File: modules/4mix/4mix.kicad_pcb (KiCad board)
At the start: 2 copper layers, 91.4 x 68.6 mm, 104 parts, among them U1 MCP6002-xSN, U2 MCP6002-xSN, U3 MCP6002-xSN, U4 MCP6002-xSN, U5 MCP6002-xSN, U6 MCP6002-xSN, U7 MCP6002-xSN, U8 MCP6002-xSN

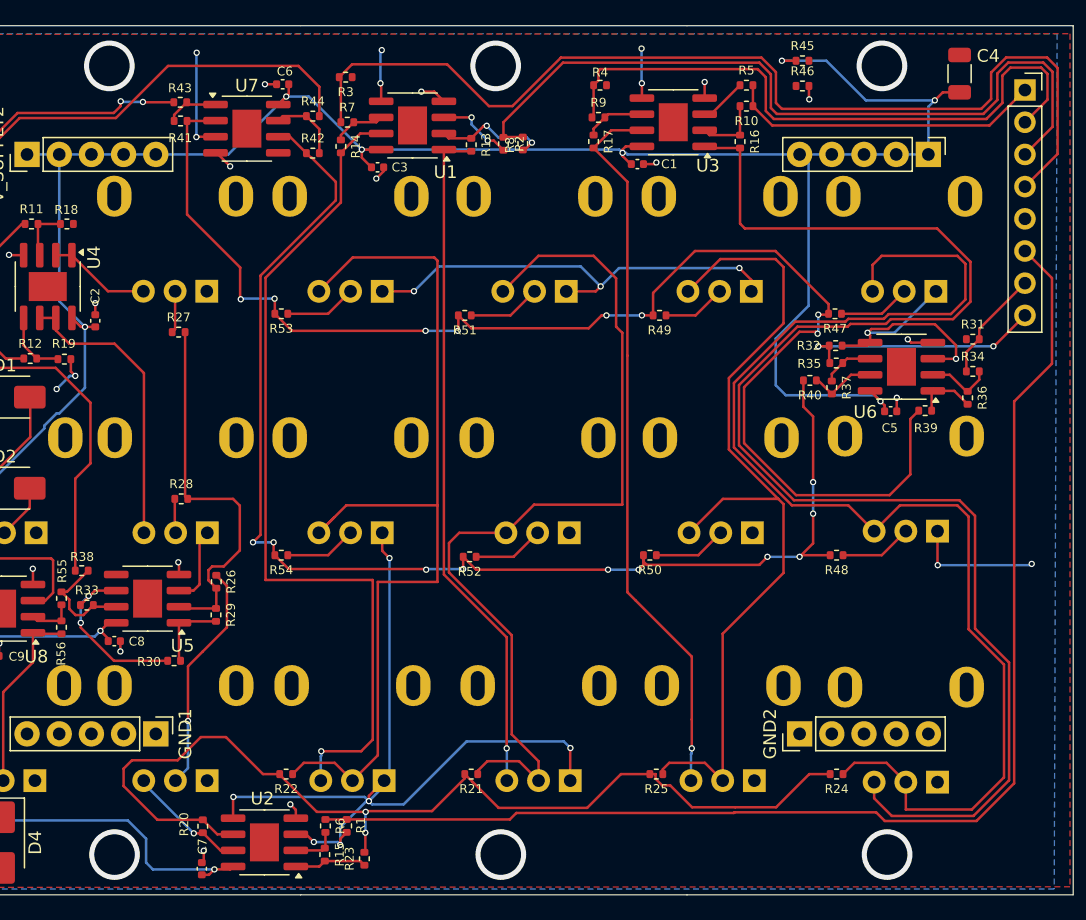
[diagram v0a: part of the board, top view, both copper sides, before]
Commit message: 4mix: Fix leaky ch1 sendA routing Also change the mounting hole positions to match mirroring
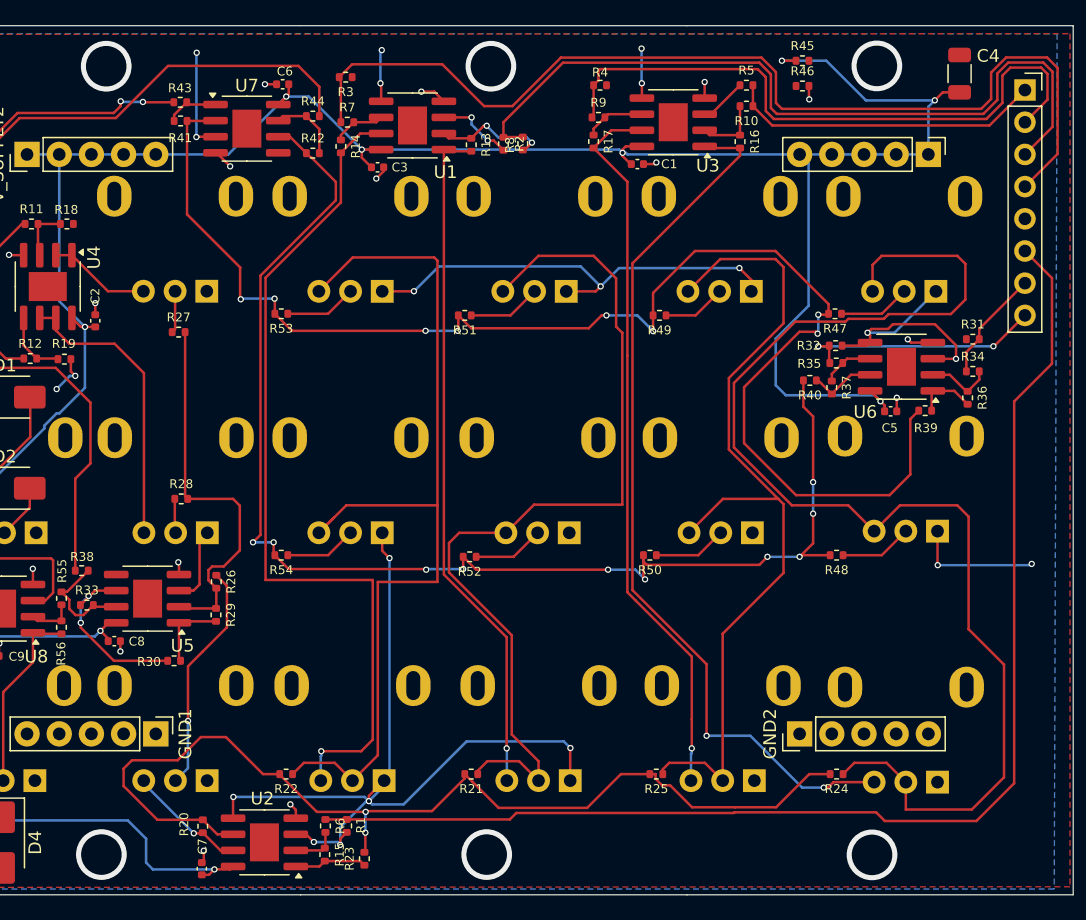
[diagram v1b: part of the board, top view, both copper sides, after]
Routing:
- net Net-(R16-Pad2): track 113.7 -> 70.3 mm, vias 0 -> 2
- net SEND_A_MIX: track 109.2 -> 110.9 mm
- net SEND_B_MIX: track 102.1 -> 103.6 mm
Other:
- board text added: "4MIX 0.3.0"
- board text removed: "4MIX 0.2.0"

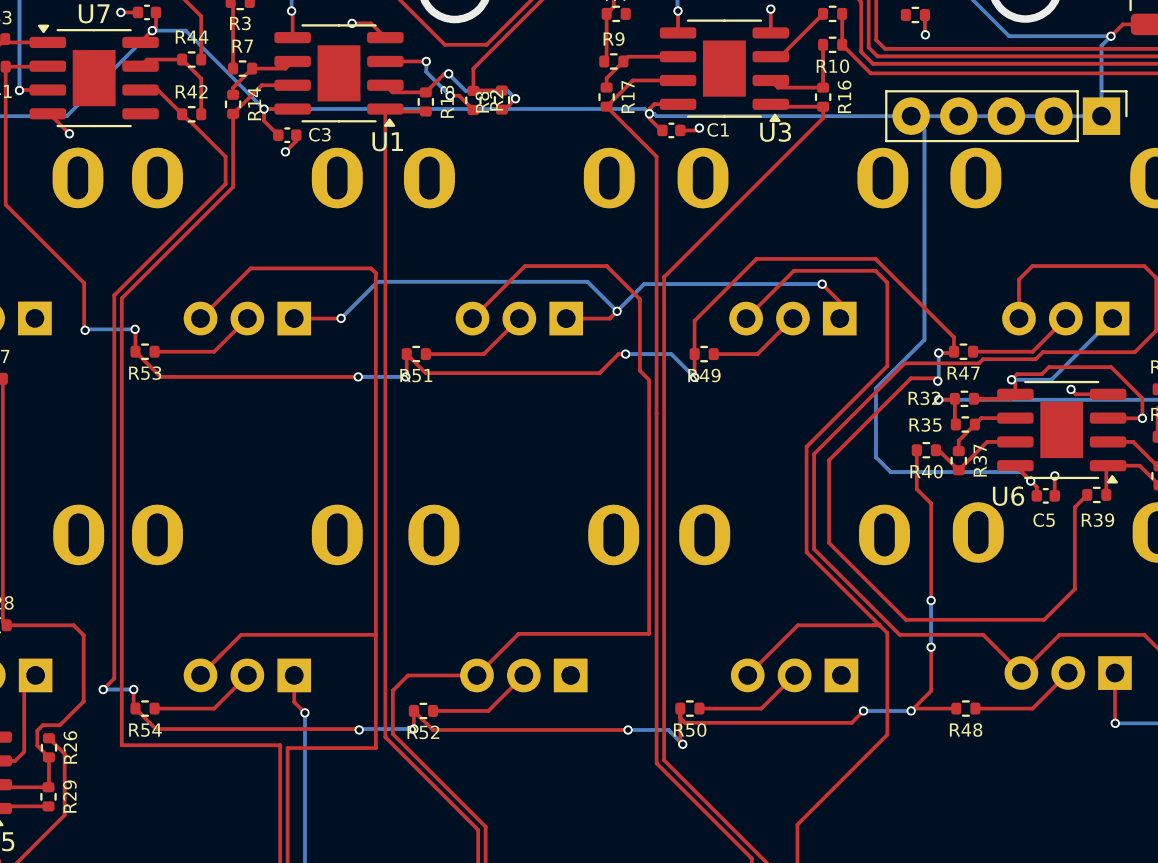
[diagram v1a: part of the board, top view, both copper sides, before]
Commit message: 4mix: Fixing ch4 send-b leakage.
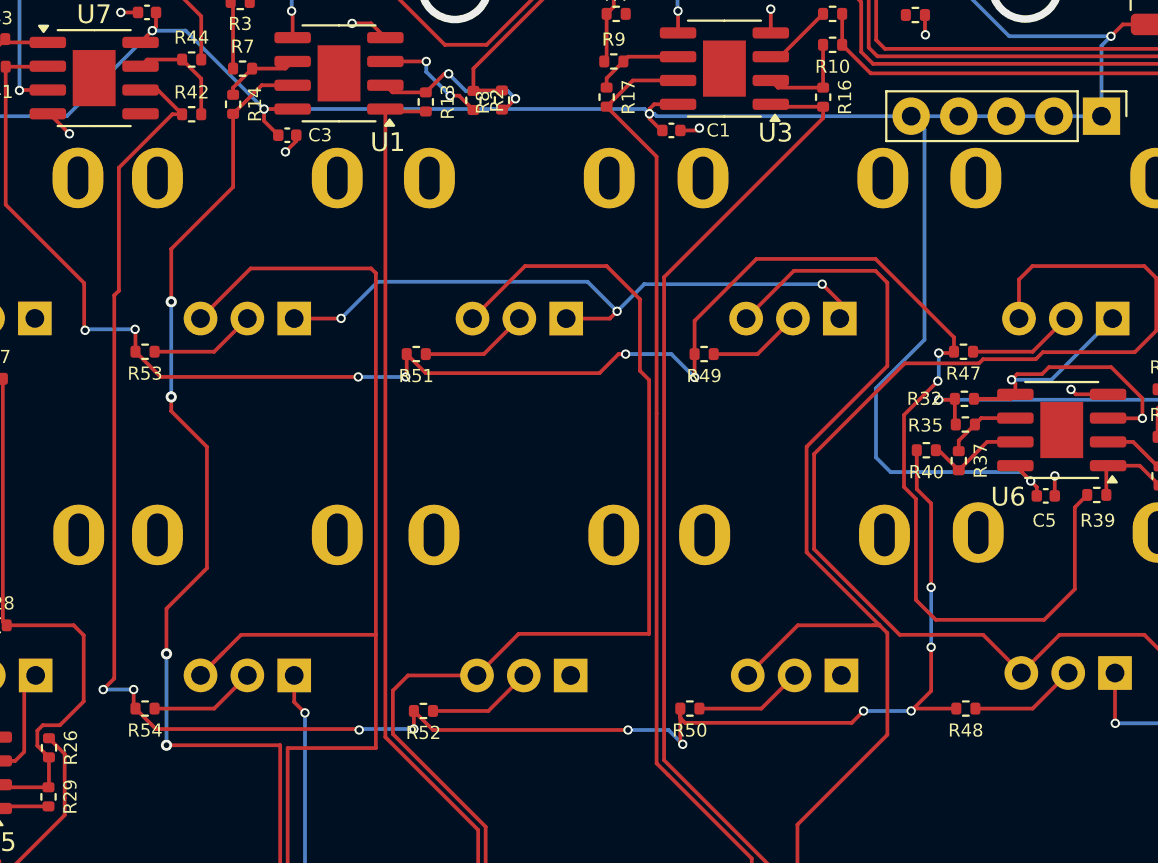
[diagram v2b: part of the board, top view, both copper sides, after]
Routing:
- net SEND_A_MIX: track 110.9 -> 105.6 mm
- net Net-(R14-Pad2): track 67.8 -> 66.0 mm, vias 1 -> 5
- net SEND_B_MIX: track 103.6 -> 101.9 mm
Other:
- board text added: "4MIX 0.4.0"
- board text removed: "4MIX 0.3.0"
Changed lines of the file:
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@@
 		)
 	)
-	(gr_text "4MIX\n0.3.0"
+	(gr_text "4MIX\n0.4.0"
 		(at 48.387 107.95 0)
 		(layer "B.SilkS")
@@
 	)
 	(segment
-		(start 116.561772 77.686)
-		(end 123.9392 77.686)
-		(width 0.2)
-		(layer "F.Cu")
-		(net 37)
-	)
-	(segment
-		(start 112.4584 69.165372)
-		(end 112.4584 73.582628)
-		(width 0.2)
-		(layer "F.Cu")
-		(net 37)
-	)
-	(segment
 		(start 108.585 58.42)
 		(end 105.279 61.726)
@@
 	)
 	(segment
+		(start 117.094 71.228486)
+		(end 117.094 76.622218)
+		(width 0.2)
+		(layer "F.Cu")
+		(net 37)
+	)
+	(segment
 		(start 76.7802 64.7192)
 		(end 75.434 63.373)
@@
 	)
 	(segment
-		(start 125.5772 76.048)
-		(end 125.5772 71.6792)
-		(width 0.2)
-		(layer "F.Cu")
-		(net 37)
-	)
-	(segment
 		(start 68.5058 48.1584)
 		(end 68.5058 55.5264)
@@
 	)
 	(segment
-		(start 116.830772 64.793)
-		(end 112.4584 69.165372)
+		(start 116.459 66.7464)
+		(end 116.459 70.593486)
 		(width 0.2)
 		(layer "F.Cu")
@@
 	)
 	(segment
+		(start 116.459 70.593486)
+		(end 117.094 71.228486)
+		(width 0.2)
+		(layer "F.Cu")
+		(net 37)
+	)
+	(segment
 		(start 114.935 58.42)
 		(end 108.585 58.42)
@@
 	)
 	(segment
+		(start 117.094 76.622218)
+		(end 118.157782 77.686)
+		(width 0.2)
+		(layer "F.Cu")
+		(net 37)
+	)
+	(segment
+		(start 118.157782 77.686)
+		(end 123.9392 77.686)
+		(width 0.2)
+		(layer "F.Cu")
+		(net 37)
+	)
+	(segment
 		(start 119.124 62.609)
 		(end 114.935 58.42)
@@
 	)
 	(segment
-		(start 112.4584 73.582628)
-		(end 116.561772 77.686)
-		(width 0.2)
-		(layer "F.Cu")
-		(net 37)
-	)
-	(segment
 		(start 75.434 62.2006)
 		(end 75.434 63.373)
@@
 	)
 	(segment
-		(start 119.054 63.443)
-		(end 119.124 63.373)
+		(start 118.2624 64.943)
+		(end 116.459 66.7464)
 		(width 0.2)
 		(layer "F.Cu")
@@
 	)
 	(segment
-		(start 123.9392 77.686)
-		(end 125.5772 76.048)
+		(start 119.054 63.443)
+		(end 119.124 63.373)
 		(width 0.2)
 		(layer "F.Cu")
@@
 	)
 	(segment
-		(start 118.2624 64.943)
-		(end 118.1124 64.793)
+		(start 125.5772 76.048)
+		(end 125.5772 71.6792)
 		(width 0.2)
 		(layer "F.Cu")
@@
 	)
 	(segment
-		(start 125.5772 71.6792)
-		(end 126.238 71.0184)
+		(start 123.9392 77.686)
+		(end 125.5772 76.048)
 		(width 0.2)
 		(layer "F.Cu")
@@
 	)
 	(segment
-		(start 101.6 63.5)
-		(end 101.219 63.5)
+		(start 125.5772 71.6792)
+		(end 126.238 71.0184)
 		(width 0.2)
 		(layer "F.Cu")
@@
 	)
 	(segment
-		(start 118.1124 64.793)
-		(end 116.830772 64.793)
+		(start 101.6 63.5)
+		(end 101.219 63.5)
 		(width 0.2)
 		(layer "F.Cu")
@@
 	)
 	(segment
+		(start 104.775 83.185)
+		(end 104.517 82.927)
+		(width 0.2)
+		(layer "F.Cu")
+		(net 41)
+	)
+	(segment
 		(start 117.9068 71.4756)
-		(end 117.9068 76.6572)
+		(end 117.1408 70.7096)
 		(width 0.2)
 		(layer "F.Cu")
@@
 	)
 	(segment
-		(start 104.775 83.185)
-		(end 104.517 82.927)
+		(start 74.3014 60.362514)
+		(end 74.549 60.114914)
 		(width 0.2)
 		(layer "F.Cu")
@@
 	)
 	(segment
-		(start 117.1408 68.6308)
-		(end 117.1408 70.7096)
+		(start 117.1408 70.7096)
+		(end 117.1408 68.6308)
 		(width 0.2)
 		(layer "F.Cu")
@@
 	)
 	(segment
+		(start 73.7108 81.407)
+		(end 74.3014 80.8164)
+		(width 0.2)
+		(layer "F.Cu")
+		(net 41)
+	)
+	(segment
 		(start 76.5262 83.5152)
 		(end 75.434 82.423)
@@
 	)
 	(segment
-		(start 80.245 54.418914)
-		(end 80.245 52.9654)
-		(width 0.2)
-		(layer "F.Cu")
-		(net 41)
-	)
-	(segment
-		(start 74.3014 60.362514)
-		(end 80.245 54.418914)
+		(start 74.549 60.114914)
+		(end 74.549 53.552405)
 		(width 0.2)
 		(layer "F.Cu")
@@
 	)
 	(segment
-		(start 104.517 84.197)
-		(end 104.517 82.423)
+		(start 74.549 53.552405)
+		(end 77.403005 50.6984)
 		(width 0.2)
 		(layer "F.Cu")
@@
 	)
 	(segment
-		(start 73.7108 81.407)
-		(end 74.3014 80.8164)
+		(start 117.9068 75.946)
+		(end 117.9068 71.4756)
 		(width 0.2)
 		(layer "F.Cu")
@@
 	)
 	(segment
-		(start 117.9068 79.1464)
-		(end 117.9068 81.4832)
+		(start 104.517 84.197)
+		(end 104.517 82.423)
 		(width 0.2)
 		(layer "F.Cu")
@@
 	)
 	(segment
-		(start 117.1408 70.7096)
-		(end 117.9068 71.4756)
+		(start 117.9068 79.1464)
+		(end 117.9068 81.4832)
 		(width 0.2)
 		(layer "F.Cu")
@@
 	)
 	(segment
-		(start 78.267 51.0422)
-		(end 77.9232 50.6984)
+		(start 74.3014 80.8164)
+		(end 74.3014 60.362514)
 		(width 0.2)
 		(layer "F.Cu")
@@
 	)
 	(segment
-		(start 80.245 52.9654)
-		(end 78.3218 51.0422)
+		(start 76.6278 49.403)
+		(end 75.7032 49.403)
 		(width 0.2)
 		(layer "F.Cu")
@@
 	)
 	(segment
-		(start 76.6278 49.403)
-		(end 75.7032 49.403)
+		(start 77.403005 50.6984)
+		(end 77.9232 50.6984)
 		(width 0.2)
 		(layer "F.Cu")
@@
 	)
 	(segment
-		(start 78.3218 51.0422)
-		(end 78.267 51.0422)
-		(width 0.2)
-		(layer "F.Cu")
-		(net 41)
-	)
-	(segment
 		(start 116.967 82.423)
 		(end 116.84 82.55)
@@
 	)
 	(segment
-		(start 74.3014 80.8164)
-		(end 74.3014 60.362514)
-		(width 0.2)
-		(layer "F.Cu")
-		(net 41)
-	)
-	(segment
 		(start 114.3 82.55)
 		(end 113.665 83.185)
@@
 	)
 	(via
-		(at 117.9068 76.6572)
+		(at 117.9068 75.946)
 		(size 0.5)
 		(drill 0.3)
@@
 	)
 	(segment
-		(start 73.7108 81.407)
-		(end 75.3364 81.407)
+		(start 117.9068 75.946)
+		(end 117.9068 79.1464)
 		(width 0.2)
 		(layer "B.Cu")
@@
 	)
 	(segment
-		(start 116.84 82.55)
-		(end 114.3 82.55)
+		(start 73.7108 81.407)
+		(end 75.3364 81.407)
 		(width 0.2)
 		(layer "B.Cu")
@@
 	)
 	(segment
-		(start 117.9068 76.6572)
-		(end 117.9068 79.1464)
+		(start 116.84 82.55)
+		(end 114.3 82.55)
 		(width 0.2)
 		(layer "B.Cu")
@@
 	)
 	(segment
+		(start 79.248 68.453)
+		(end 79.248 74.93)
+		(width 0.2)
+		(layer "F.Cu")
+		(net 45)
+	)
+	(segment
+		(start 77.343 57.8866)
+		(end 77.343 60.706)
+		(width 0.2)
+		(layer "F.Cu")
+		(net 45)
+	)
+	(segment
+		(start 77.089 77.089)
+		(end 77.089 79.502)
+		(width 0.2)
+		(layer "F.Cu")
+		(net 45)
+	)
+	(segment
 		(start 80.645 50.677)
 		(end 82.173 49.149)
@@
 	)
 	(segment
-		(start 74.7014 84.3788)
-		(end 83.157 84.3788)
+		(start 80.645 54.5846)
+		(end 77.343 57.8866)
+		(width 0.2)
+		(layer "F.Cu")
+		(net 45)
+	)
+	(segment
+		(start 77.343 66.548)
+		(end 79.248 68.453)
+		(width 0.2)
+		(layer "F.Cu")
+		(net 45)
+	)
+	(segment
+		(start 79.121 75.057)
+		(end 77.089 77.089)
 		(width 0.2)
 		(layer "F.Cu")
@@
 	)
 	(segment
-		(start 80.645 54.5846)
-		(end 74.7014 60.5282)
+		(start 79.248 74.93)
+		(end 79.121 75.057)
 		(width 0.2)
 		(layer "F.Cu")
@@
 	)
 	(segment
-		(start 74.7014 60.5282)
-		(end 74.7014 84.3788)
+		(start 77.089 84.3788)
+		(end 83.157 84.3788)
+		(width 0.2)
+		(layer "F.Cu")
+		(net 45)
+	)
+	(segment
+		(start 77.343 65.786)
+		(end 77.343 66.548)
 		(width 0.2)
 		(layer "F.Cu")
@@
 	)
 	(via
+		(at 77.089 84.3788)
+		(size 0.6)
+		(drill 0.3)
+		(layers "F.Cu" "B.Cu")
+		(net 45)
+	)
+	(via
 		(at 79.0956 97.8916)
 		(size 0.5)
@@
 		(net 45)
 	)
+	(via
+		(at 77.089 79.502)
+		(size 0.6)
+		(drill 0.3)
+		(layers "F.Cu" "B.Cu")
+		(net 45)
+	)
+	(via
+		(at 77.343 65.786)
+		(size 0.6)
+		(drill 0.3)
+		(layers "F.Cu" "B.Cu")
+		(net 45)
+	)
+	(via
+		(at 77.343 60.706)
+		(size 0.6)
+		(drill 0.3)
+		(layers "F.Cu" "B.Cu")
+		(net 45)
+	)
+	(segment
+		(start 77.343 60.706)
+		(end 77.343 65.786)
+		(width 0.2)
+		(layer "B.Cu")
+		(net 45)
+	)
+	(segment
+		(start 77.089 79.502)
+		(end 77.089 84.3788)
+		(width 0.2)
+		(layer "B.Cu")
+		(net 45)
+	)

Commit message: Finished the new schematic for 4mix
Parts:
- removed C1, C2, C3, C5, C6, C7, C8, C9: 0.1uf, Capacitor_SMD:C_0402_1005Metric
- removed C4: 100uf, Capacitor_SMD:C_1206_3216Metric
- removed D1, D2, D3: SS14, Diode_SMD:D_SMA
- removed D4: SS210, Diode_SMD:D_SMA
- removed R1, R18, R19, R2, R3, R31, R32, R39, R4, R40, R41, R42, R47, R48, R49, R5, R50, R51, R52, R53, R54: 1M, Resistor_SMD:R_0402_1005Metric
- removed R10, R11, R12, R13, R14, R15, R16, R17, R30, R33, R34, R35, R36, R37, R55, R56, R6, R7, R8, R9: 100k, Resistor_SMD:R_0402_1005Metric
- removed R20, R21, R22, R23, R24, R25, R26, R27, R28, R29: 200k, Resistor_SMD:R_0402_1005Metric
- removed R38, R43, R44, R45, R46, R57, R59, R60: 1k, Resistor_SMD:R_0402_1005Metric
- removed R58: 51k, Resistor_SMD:R_0402_1005Metric
- removed RV1, RV16, RV2, RV3, RV4, RV5, RV6, RV7: 50k, BreadModular_Pots:Potentiometer_RV09
- removed RV10, RV11, RV12, RV13, RV14, RV15, RV17, RV8, RV9: 500k, BreadModular_Pots:Potentiometer_RV09
- removed U1, U2, U3, U4, U5, U6, U7, U8: MCP6002-xSN, Package_SO:SOIC-8-1EP_3.9x4.9mm_P1.27mm_EP2.29x3mm
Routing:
- net V_SUPPLY: track 240.0 -> 0.00 mm, vias 10 -> 0
- net V_MID: track 180.1 -> 0.00 mm, vias 24 -> 1
- net SEND_A_MIX: track 105.6 -> 0.00 mm, vias 8 -> 0
- net SEND_B_MIX: track 101.9 -> 0.00 mm, vias 10 -> 0
- net IN_MIXOUT: track 100.2 -> 0.00 mm
- net /SENDS/INPUT: track 100.1 -> 0.00 mm
- net IN_4: track 80.4 -> 0.00 mm
- net MAIN_MIX: track 80.1 -> 0.00 mm, vias 2 -> 0
- net /SENDS3/INPUT: track 74.8 -> 0.00 mm
- net /SENDS2/INPUT: track 71.5 -> 0.00 mm
- net Net-(R16-Pad2): track 70.3 -> 0.00 mm, vias 2 -> 0
- net /SENDS1/INPUT: track 69.3 -> 0.00 mm
- net Net-(R14-Pad2): track 66.0 -> 0.00 mm, vias 5 -> 0
- net IN_3: track 61.9 -> 0.00 mm
- net Net-(R17-Pad2): track 57.5 -> 0.00 mm, vias 1 -> 0
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- removed copper zone on B.Cu, net GND
- removed copper zone on F.Cu, net V_MID
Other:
- board text removed: "CH-1"
- board text removed: "CH-2"
- board text removed: "CH-3"
- board text removed: "CH-4"
- board text removed: "RETURN A"
- board text removed: "RETURN B"
- board text removed: "SA"
- board text removed: "SB"
- board text removed: "SEND A"
- board text removed: "SEND B"

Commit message: Add base setup for routing
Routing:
- added copper zone on In1.Cu, net GND
- added copper zone on B.Cu, net V_SUPPLY
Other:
- copper layers 2 -> 4
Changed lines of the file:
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@@
 	(layers
 		(0 "F.Cu" signal)
+		(4 "In1.Cu" signal)
+		(6 "In2.Cu" signal)
 		(2 "B.Cu" signal)
 		(9 "F.Adhes" user "F.Adhesive")
@@
 			)
 			(layer "dielectric 1"
+				(type "prepreg")
+				(thickness 0.1)
+				(material "FR4")
+				(epsilon_r 4.5)
+				(loss_tangent 0.02)
+			)
+			(layer "In1.Cu"
+				(type "copper")
+				(thickness 0.035)
+			)
+			(layer "dielectric 2"
 				(type "core")
-				(thickness 1.51)
+				(thickness 1.24)
+				(material "FR4")
+				(epsilon_r 4.5)
+				(loss_tangent 0.02)
+			)
+			(layer "In2.Cu"
+				(type "copper")
+				(thickness 0.035)
+			)
+			(layer "dielectric 3"
+				(type "prepreg")
+				(thickness 0.1)
 				(material "FR4")
 				(epsilon_r 4.5)
@@
 		(net 0)
 		(net_name "")
-		(layer "F.Cu")
+		(layers "F.Cu" "B.Cu" "In1.Cu" "In2.Cu")
 		(hatch edge 0.5)
 		(connect_pads
@@
 		(placement
 			(enabled no)
-			(sheetname "")
+			(sheetname "Root")
 		)
 		(fill
@@
 		(polygon
 			(pts
-				(xy 53.975 48.895) (xy 67.31 48.895) (xy 67.31 52.705) (xy 53.975 52.705)
+				(xy 48.895 43.815) (xy 52.705 43.815) (xy 52.7812 65.7098) (xy 48.9712 65.7098)
 			)
 		)
@@
 		(net 0)
 		(net_name "")
-		(layer "F.Cu")
+		(layers "F.Cu" "B.Cu" "In1.Cu" "In2.Cu")
 		(hatch edge 0.5)
 		(connect_pads
@@
 		(placement
 			(enabled no)
-			(sheetname "")
+			(sheetname "Root")
 		)
 		(fill
@@
 		(polygon
 			(pts
-				(xy 114.935 94.615) (xy 128.905 94.615) (xy 128.905 98.425) (xy 114.935 98.425)
+				(xy 132.715 43.815) (xy 136.525 43.815) (xy 136.525 65.405) (xy 132.715 65.405)
 			)
 		)
@@
 		(net 0)
 		(net_name "")
-		(layer "F.Cu")
+		(layers "F.Cu" "B.Cu" "In2.Cu")
 		(hatch edge 0.5)
 		(connect_pads
@@
 		(placement
 			(enabled no)
-			(sheetname "")
+			(sheetname "Root")
 		)
 		(fill
@@
 		(polygon
 			(pts
-				(xy 53.975 94.615) (xy 67.945 94.615) (xy 67.945 98.425) (xy 53.975 98.425)
+				(xy 114.935 94.615) (xy 128.905 94.615) (xy 128.905 98.425) (xy 114.935 98.425)
 			)
 		)
@@
 		(net 0)
 		(net_name "")
-		(layer "F.Cu")
+		(layers "F.Cu" "B.Cu" "In2.Cu")
 		(hatch edge 0.5)
 		(connect_pads
@@
 		(placement
 			(enabled no)
-			(sheetname "")
+			(sheetname "Root")
 		)
 		(fill
@@
 		(polygon
 			(pts
-				(xy 114.935 48.895) (xy 128.905 48.895) (xy 128.905 52.705) (xy 114.935 52.705)
+				(xy 53.975 94.615) (xy 67.945 94.615) (xy 67.945 98.425) (xy 53.975 98.425)
 			)
 		)
@@
 		(net 0)
 		(net_name "")
-		(layers "F.Cu" "B.Cu")
+		(layers "F.Cu" "In1.Cu" "In2.Cu")
 		(hatch edge 0.5)
 		(connect_pads
@@
 		(placement
 			(enabled no)
-			(sheetname "")
+			(sheetname "Root")
 		)
 		(fill
@@
 		(polygon
 			(pts
-				(xy 48.895 43.815) (xy 52.705 43.815) (xy 52.7812 65.7098) (xy 48.9712 65.7098)
+				(xy 53.975 48.895) (xy 67.945 48.895) (xy 67.945 52.705) (xy 53.975 52.705)
 			)
 		)
@@
 		(net 0)
 		(net_name "")
-		(layers "F.Cu" "B.Cu")
+		(layers "F.Cu" "In1.Cu" "In2.Cu")
 		(hatch edge 0.5)
 		(connect_pads
@@
 		(placement
 			(enabled no)
-			(sheetname "")
+			(sheetname "Root")
 		)
 		(fill
@@
 		(polygon
 			(pts
-				(xy 132.715 43.815) (xy 136.525 43.815) (xy 136.525 65.405) (xy 132.715 65.405)
-			)
-		)
+				(xy 114.935 48.895) (xy 128.905 48.895) (xy 128.905 52.705) (xy 114.935 52.705)
+			)
+		)
+	)
+	(zone
+		(net 9)
+		(net_name "V_SUPPLY")
+		(layer "B.Cu")
+		(hatch edge 0.5)
+		(priority 1)
+		(connect_pads
+			(clearance 0)
+		)
+		(min_thickness 0.25)
+		(filled_areas_thickness no)
+		(fill yes
+			(thermal_gap 0.5)
+			(thermal_bridge_width 0.5)
+		)
+		(polygon
+			(pts
+				(xy 137.668 41.656) (xy 137.6172 108.2548) (xy 47.752 108.204) (xy 47.752 41.656)
+			)
+		)
+	)
+	(zone
+		(net 1)
+		(net_name "GND")
+		(layer "In1.Cu")
+		(hatch edge 0.5)
+		(connect_pads
+			(clearance 0)
+		)
+		(min_thickness 0.25)
+		(filled_areas_thickness no)
+		(fill yes
+			(thermal_gap 0.5)
+			(thermal_bridge_width 0.5)
+		)
+		(polygon
+			(pts
+				(xy 47.8028 41.656) (xy 137.7188 41.656) (xy 137.668 108.2548) (xy 131.3688 108.8136) (xy 47.7012 108.712)
+			)
+		)
